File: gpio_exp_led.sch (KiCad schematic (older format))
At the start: 30 parts, among them U1 PCA9552PW,118, U2 PCA9552PW,118, U3 PCA9552PW,118, U4 PCA9552PW,118

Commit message: 64 port hat
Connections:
- net pwr_toggle_00: now also U1.11 (LED7); no longer U1.4 (LED0)
- net pwr_toggle_01: now also U1.10 (LED6); no longer U1.5 (LED1)
- net pwr_toggle_02: now also U1.9 (LED5); no longer U1.6 (LED2)
- net pwr_toggle_03: now also U1.8 (LED4); no longer U1.7 (LED3)
- net pwr_toggle_04: now also U1.7 (LED3); no longer U1.8 (LED4)
- net pwr_toggle_05: now also U1.6 (LED2); no longer U1.9 (LED5)
- net pwr_toggle_06: now also U1.5 (LED1); no longer U1.10 (LED6)
- net pwr_toggle_07: now also U1.4 (LED0); no longer U1.11 (LED7)
- net pwr_toggle_16: now also U2.11 (LED7); no longer U2.4 (LED0)
- net pwr_toggle_17: now also U2.10 (LED6); no longer U2.5 (LED1)
- net pwr_toggle_18: now also U2.9 (LED5); no longer U2.6 (LED2)
- net pwr_toggle_19: now also U2.8 (LED4); no longer U2.7 (LED3)
- net pwr_toggle_20: now also U2.7 (LED3); no longer U2.8 (LED4)
- net pwr_toggle_21: now also U2.6 (LED2); no longer U2.9 (LED5)
- net pwr_toggle_22: now also U2.5 (LED1); no longer U2.10 (LED6)
- net pwr_toggle_23: now also U2.4 (LED0); no longer U2.11 (LED7)
- net pwr_toggle_32: now also U3.11 (LED7); no longer U3.4 (LED0)
- net pwr_toggle_33: now also U3.10 (LED6); no longer U3.5 (LED1)
- net pwr_toggle_34: now also U3.9 (LED5); no longer U3.6 (LED2)
- net pwr_toggle_35: now also U3.8 (LED4); no longer U3.7 (LED3)
- net pwr_toggle_36: now also U3.7 (LED3); no longer U3.8 (LED4)
- net pwr_toggle_37: now also U3.6 (LED2); no longer U3.9 (LED5)
- net pwr_toggle_38: now also U3.5 (LED1); no longer U3.10 (LED6)
- net pwr_toggle_39: now also U3.4 (LED0); no longer U3.11 (LED7)
- net pwr_toggle_48: now also U4.11 (LED7); no longer U4.4 (LED0)
- net pwr_toggle_49: now also U4.10 (LED6); no longer U4.5 (LED1)
- net pwr_toggle_50: now also U4.9 (LED5); no longer U4.6 (LED2)
- net pwr_toggle_51: now also U4.8 (LED4); no longer U4.7 (LED3)
- net pwr_toggle_52: now also U4.7 (LED3); no longer U4.8 (LED4)
- net pwr_toggle_53: now also U4.6 (LED2); no longer U4.9 (LED5)
- net pwr_toggle_54: now also U4.5 (LED1); no longer U4.10 (LED6)
- net pwr_toggle_55: now also U4.4 (LED0); no longer U4.11 (LED7)
- net GPIO17_GEN0 renamed GPIO_RST_0
- net GPIO18_GEN1 renamed GPIO_RST_1
- net GPIO22_GEN3 renamed GPIO_RST_3
- net GPIO27_GEN2 renamed GPIO_RST_2
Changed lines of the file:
@@
 Wire Wire Line
 	2850 2025 2975 2025
-Text Label 2850 2225 0    50   ~ 0
-SDA
-Text Label 2850 2325 0    50   ~ 0
-SCL
-Wire Wire Line
-	3075 2325 2850 2325
-Wire Wire Line
-	2850 2225 3075 2225
 $Comp
 L atv_cluster_hat:PCA9552PW,118 U2
@@
 	6250 1200 6250 1550
 Wire Wire Line
-	6125 2050 6225 2050
-Text Label 6125 2250 0    50   ~ 0
-SDA
-Text Label 6125 2350 0    50   ~ 0
-SCL
+	6125 2050 6180 2050
 Wire Wire Line
 	6350 2350 6125 2350
@@
 	3050 4025 3050 4375
 Wire Wire Line
-	2925 4875 3025 4875
-Text Label 2925 5075 0    50   ~ 0
-SDA
-Text Label 2925 5175 0    50   ~ 0
-SCL
-Wire Wire Line
 	3150 5175 2925 5175
 Wire Wire Line
@@
 Wire Wire Line
 	6200 4900 6300 4900
-Text Label 6200 5100 0    50   ~ 0
-SDA
-Text Label 6200 5200 0    50   ~ 0
-SCL
 Wire Wire Line
 	6425 5200 6200 5200
@@
 Wire Wire Line
 	5625 4600 5875 4600
-Text Label 1675 2150 0    50   ~ 0
-GPIO17_GEN0
-Text Label 1750 5000 0    50   ~ 0
-GPIO27_GEN2
-Text Label 6000 5100 2    50   ~ 0
-GPIO22_GEN3
 Wire Wire Line
 	2650 2150 2650 2100
@@
 Wire Wire Line
 	2975 2100 2975 2025
-Wire Wire Line
-	1675 2150 2650 2150
 Connection ~ 2975 2025
 Wire Wire Line
 	2975 2025 3075 2025
-Text Label 5325 2225 0    50   ~ 0
-GPIO18_GEN1
-Wire Wire Line
-	5325 2225 5875 2225
-Wire Wire Line
-	5875 2225 5875 2125
-Wire Wire Line
-	5875 2125 6225 2125
-Wire Wire Line
-	6225 2125 6225 2050
-Connection ~ 6225 2050
-Wire Wire Line
-	6225 2050 6350 2050
-Wire Wire Line
-	2875 5000 2875 4950
-Wire Wire Line
-	2875 4950 3025 4950
-Wire Wire Line
-	3025 4950 3025 4875
-Wire Wire Line
-	1750 5000 2875 5000
-Connection ~ 3025 4875
-Wire Wire Line
-	3025 4875 3150 4875
-Wire Wire Line
-	6000 5100 6075 5100
 Wire Wire Line
 	6075 5100 6075 5000
@@
 Wire Wire Line
 	6300 4900 6425 4900
-Text Label 8925 5200 0    50   ~ 0
-SDA
-Text Label 8925 5300 0    50   ~ 0
-SCL
 $Comp
 L Device:R R?
@@
 Text Notes 8775 5500 0    50   ~ 0
 Place second set of pull ups\n at final gpio expander
+Text GLabel 4550 2225 2    20   Input ~ 0
+pwr_toggle_00
+Text GLabel 4550 2125 2    20   Input ~ 0
+pwr_toggle_01
+Text GLabel 4550 2025 2    20   Input ~ 0
+pwr_toggle_02
+Text GLabel 4550 1925 2    20   Input ~ 0
+pwr_toggle_03
+Text GLabel 4550 1825 2    20   Input ~ 0
+pwr_toggle_04
+Text GLabel 4550 1725 2    20   Input ~ 0
+pwr_toggle_05
+Text GLabel 4550 1625 2    20   Input ~ 0
+pwr_toggle_06
 Text GLabel 4550 1525 2    20   Input ~ 0
-pwr_toggle_00
-Text GLabel 4550 1625 2    20   Input ~ 0
-pwr_toggle_01
-Text GLabel 4550 1725 2    20   Input ~ 0
-pwr_toggle_02
-Text GLabel 4550 1825 2    20   Input ~ 0
-pwr_toggle_03
-Text GLabel 4550 1925 2    20   Input ~ 0
-pwr_toggle_04
-Text GLabel 4550 2025 2    20   Input ~ 0
-pwr_toggle_05
-Text GLabel 4550 2125 2    20   Input ~ 0
-pwr_toggle_06
-Text GLabel 4550 2225 2    20   Input ~ 0
 pwr_toggle_07
 Text GLabel 4550 2325 2    20   Input ~ 0
@@
 Wire Wire Line
 	4475 3025 4550 3025
+Text GLabel 7825 2250 2    20   Input ~ 0
+pwr_toggle_16
+Text GLabel 7825 2150 2    20   Input ~ 0
+pwr_toggle_17
+Text GLabel 7825 2050 2    20   Input ~ 0
+pwr_toggle_18
+Text GLabel 7825 1950 2    20   Input ~ 0
+pwr_toggle_19
+Text GLabel 7825 1850 2    20   Input ~ 0
+pwr_toggle_20
+Text GLabel 7825 1750 2    20   Input ~ 0
+pwr_toggle_21
+Text GLabel 7825 1650 2    20   Input ~ 0
+pwr_toggle_22
 Text GLabel 7825 1550 2    20   Input ~ 0
-pwr_toggle_16
-Text GLabel 7825 1650 2    20   Input ~ 0
-pwr_toggle_17
-Text GLabel 7825 1750 2    20   Input ~ 0
-pwr_toggle_18
-Text GLabel 7825 1850 2    20   Input ~ 0
-pwr_toggle_19
-Text GLabel 7825 1950 2    20   Input ~ 0
-pwr_toggle_20
-Text GLabel 7825 2050 2    20   Input ~ 0
-pwr_toggle_21
-Text GLabel 7825 2150 2    20   Input ~ 0
-pwr_toggle_22
-Text GLabel 7825 2250 2    20   Input ~ 0
 pwr_toggle_23
 Text GLabel 7825 2350 2    20   Input ~ 0
@@
 Wire Wire Line
 	7750 3050 7825 3050
+Text GLabel 4625 5075 2    20   Input ~ 0
+pwr_toggle_32
+Text GLabel 4625 4975 2    20   Input ~ 0
+pwr_toggle_33
+Text GLabel 4625 4875 2    20   Input ~ 0
+pwr_toggle_34
+Text GLabel 4625 4775 2    20   Input ~ 0
+pwr_toggle_35
+Text GLabel 4625 4675 2    20   Input ~ 0
+pwr_toggle_36
+Text GLabel 4625 4575 2    20   Input ~ 0
+pwr_toggle_37
+Text GLabel 4625 4475 2    20   Input ~ 0
+pwr_toggle_38
 Text GLabel 4625 4375 2    20   Input ~ 0
-pwr_toggle_32
-Text GLabel 4625 4475 2    20   Input ~ 0
-pwr_toggle_33
-Text GLabel 4625 4575 2    20   Input ~ 0
-pwr_toggle_34
-Text GLabel 4625 4675 2    20   Input ~ 0
-pwr_toggle_35
-Text GLabel 4625 4775 2    20   Input ~ 0
-pwr_toggle_36
-Text GLabel 4625 4875 2    20   Input ~ 0
-pwr_toggle_37
-Text GLabel 4625 4975 2    20   Input ~ 0
-pwr_toggle_38
-Text GLabel 4625 5075 2    20   Input ~ 0
 pwr_toggle_39
 Text GLabel 4625 5175 2    20   Input ~ 0
@@
 Wire Wire Line
 	4550 5875 4625 5875
+Text GLabel 7900 5100 2    20   Input ~ 0
+pwr_toggle_48
+Text GLabel 7900 5000 2    20   Input ~ 0
+pwr_toggle_49
+Text GLabel 7900 4900 2    20   Input ~ 0
+pwr_toggle_50
+Text GLabel 7900 4800 2    20   Input ~ 0
+pwr_toggle_51
+Text GLabel 7900 4700 2    20   Input ~ 0
+pwr_toggle_52
+Text GLabel 7900 4600 2    20   Input ~ 0
+pwr_toggle_53
+Text GLabel 7900 4500 2    20   Input ~ 0
+pwr_toggle_54
 Text GLabel 7900 4400 2    20   Input ~ 0
-pwr_toggle_48
-Text GLabel 7900 4500 2    20   Input ~ 0
-pwr_toggle_49
-Text GLabel 7900 4600 2    20   Input ~ 0
-pwr_toggle_50
-Text GLabel 7900 4700 2    20   Input ~ 0
-pwr_toggle_51
-Text GLabel 7900 4800 2    20   Input ~ 0
-pwr_toggle_52
-Text GLabel 7900 4900 2    20   Input ~ 0
-pwr_toggle_53
-Text GLabel 7900 5000 2    20   Input ~ 0
-pwr_toggle_54
-Text GLabel 7900 5100 2    20   Input ~ 0
 pwr_toggle_55
 Text GLabel 7900 5200 2    20   Input ~ 0
@@
 Wire Wire Line
 	7825 5900 7900 5900
+Text GLabel 2600 2150 0    20   Input ~ 0
+GPIO_RST_0
+Text GLabel 5920 2170 0    20   Input ~ 0
+GPIO_RST_1
+Text GLabel 5980 5100 0    20   Input ~ 0
+GPIO_RST_3
+Wire Wire Line
+	2600 2150 2650 2150
+Wire Wire Line
+	5920 2170 6180 2170
+Wire Wire Line
+	6180 2170 6180 2050
+Connection ~ 6180 2050
+Wire Wire Line
+	6180 2050 6350 2050
+Text GLabel 2730 4970 0    20   Input ~ 0
+GPIO_RST_2
+Wire Wire Line
+	2925 4875 2990 4875
+Wire Wire Line
+	2730 4970 2990 4970
+Wire Wire Line
+	2990 4970 2990 4875
+Connection ~ 2990 4875
+Wire Wire Line
+	2990 4875 3150 4875
+Wire Wire Line
+	5980 5100 6075 5100
+Text GLabel 2835 2225 0    20   Input ~ 0
+SDA
+Wire Wire Line
+	2835 2225 3075 2225
+Text GLabel 2835 2325 0    20   Input ~ 0
+SCL
+Wire Wire Line
+	2835 2325 3075 2325
+Text GLabel 6125 2250 0    20   Input ~ 0
+SDA
+Text GLabel 6125 2350 0    20   Input ~ 0
+SCL
+Text GLabel 2925 5075 0    20   Input ~ 0
+SDA
+Text GLabel 2925 5175 0    20   Input ~ 0
+SCL
+Text GLabel 6200 5100 0    20   Input ~ 0
+SDA
+Text GLabel 6200 5200 0    20   Input ~ 0
+SCL
+Text GLabel 8925 5200 0    20   Input ~ 0
+SDA
+Text GLabel 8925 5300 0    20   Input ~ 0
+SCL
 $EndSCHEMATC

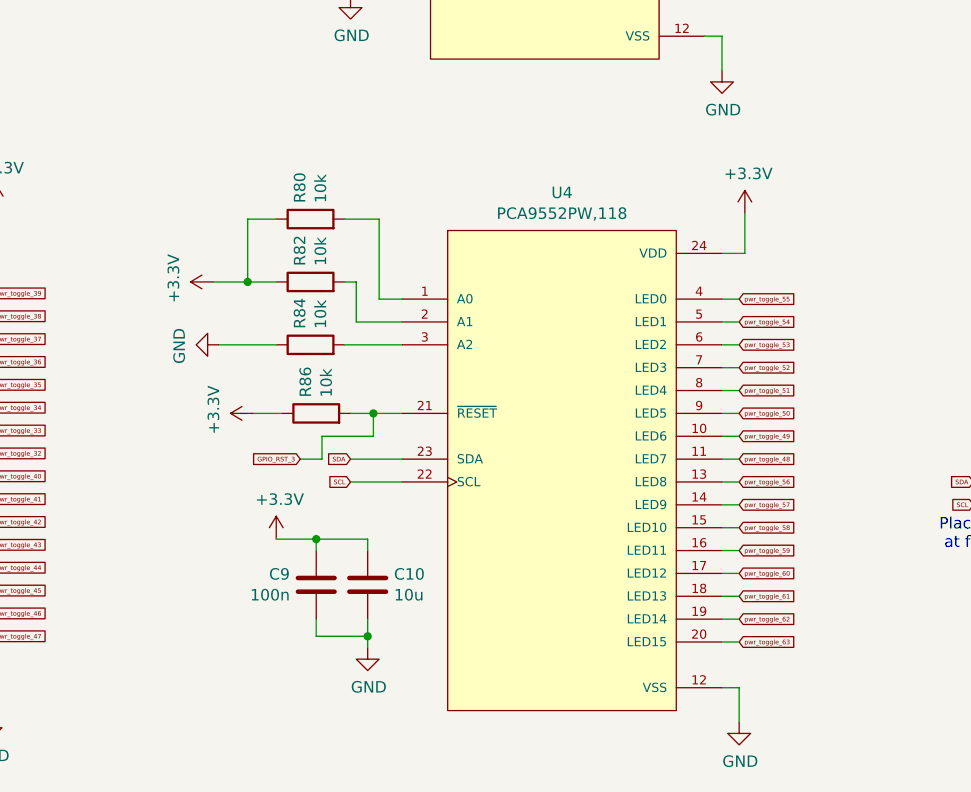
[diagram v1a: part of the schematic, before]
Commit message: PCB routed for 48 ports
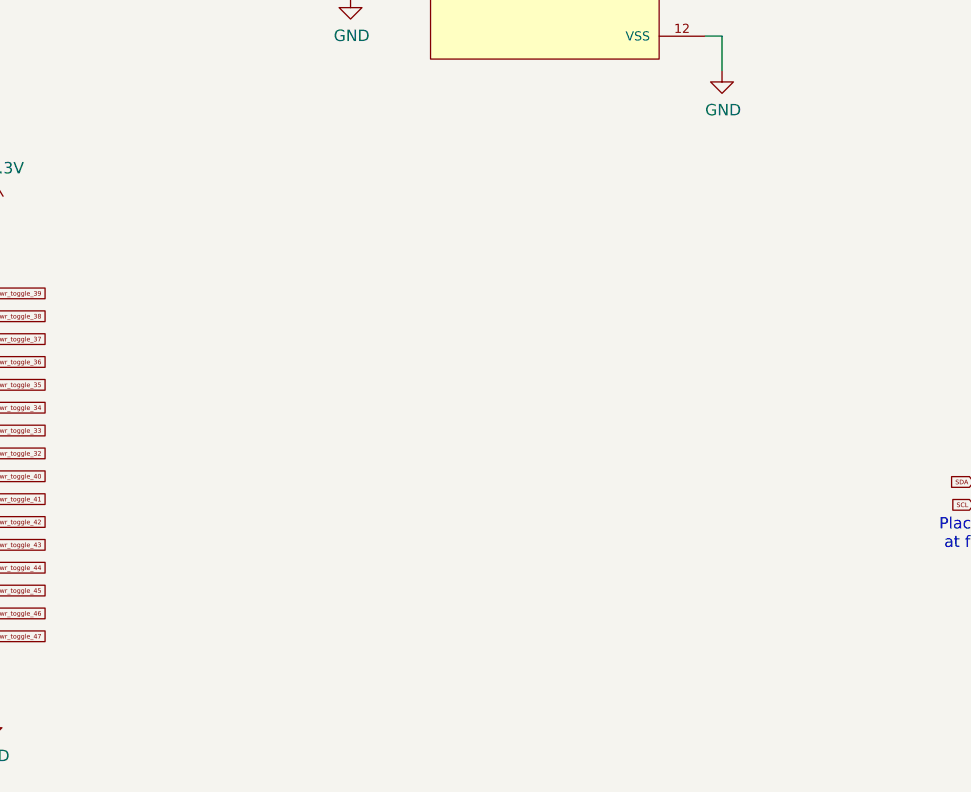
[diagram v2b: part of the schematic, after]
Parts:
- removed C10: 10u, Capacitor_SMD:C_1206_3216Metric_Pad1.42x1.75mm_HandSolder, symbol Device:C
- removed C9: 100n, Capacitor_SMD:C_1206_3216Metric_Pad1.42x1.75mm_HandSolder, symbol Device:C
- removed R80, R82, R84, R86: 10k, Resistor_SMD:R_1206_3216Metric_Pad1.42x1.75mm_HandSolder, symbol Device:R
- removed U4: PCA9552PW,118, lib:SOP65P640X110-24N, symbol atv_cluster_hat:PCA9552PW,118
